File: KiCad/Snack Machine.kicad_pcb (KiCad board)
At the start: 2 copper layers, 107.5 x 100 mm, 318 parts, among them J1 MDB, J10 Row Screw Terminal, J11 Column Screw Terminal, J12 Display Serial Header, J13 RFID_CONNECTOR, J14 Large Display Header, J16 USB_B_Micro, J17 AVR-ISP-6, J18 Conn_02x02_Odd_Even, J2 Power Screw Terminal, J3 RFID Serial Connector, J4 RFID Led Connector, J5 MDB, J6 Conn_01x02, J7 LCD EXP1, J8 LCD EXP2, J9 AVR-ISP-6, Q1 P-CH 30V 3.8A, Q10 MMBT3904, Q11 P-CH 30V 3.8A, Q12 P-CH 30V 3.8A, Q13 P-CH 30V 3.8A, Q14 P-CH 30V 3.8A, Q15 MMBT3904, Q16 MMBT3904, Q17 MMBT3904, Q18 MMBT3904, Q19 Q_NMOS_SGD, Q2 Q_NMOS_SGD, Q20 Q_NMOS_SGD, Q21 Q_NMOS_SGD, Q22 Q_NMOS_SGD, Q23 Q_NMOS_SGD, Q24 Q_NMOS_SGD, Q25 Q_NMOS_SGD, Q26 MMBT3904, Q3 P-CH 30V 3.8A, Q4 P-CH 30V 3.8A, Q5 P-CH 30V 3.8A, Q6 P-CH 30V 3.8A, Q7 MMBT3904, Q8 MMBT3904, Q9 MMBT3904, SW1 SW_SPST, U1 MEZD71201A-F, U2 MEZD71202A-G, U3 ATmega2560-16AU, U4 INA180B3, U5 INA219, U6 ATmega16U2-MU, U7 74AHC1G125, U8 W5500, U9 RB1-125BAG1A, Y1 16MHz, Y2 16MHz, Y3 25MHz

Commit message: tweaked
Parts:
- moved C24 0.50 mm to (109.3, 84.9)
- moved C26 0.50 mm to (109.3, 86.6)
- moved F2 0.50 mm to (107.3, 90.3)
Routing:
- added copper zone on B.Cu, net GND
- removed copper zone on B.Cu, net (none)
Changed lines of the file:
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@@
     (thickness 1.6)
     (drawings 12)
-    (tracks 2542)
+    (tracks 2543)
     (zones 0)
     (modules 318)
@@
     (add_net /USB_Serial/TXL)
     (add_net /USB_Serial/TX_USB)
-    (add_net /USB_Serial/USBVCC)
     (add_net /USB_Serial/USB_D+)
     (add_net /USB_Serial/USB_D-)
@@
     (add_net +3V3)
     (add_net +5V)
+    (add_net /USB_Serial/USBVCC)
     (add_net GND)
     (add_net VCC)
@@
   )
   (module "Snack Machine:MF-MSMF050-2" (layer F.Cu)
-    (at 107.3 90.763 270)
+    (at 107.3 90.263 270)
     (fp_text reference F2 (at -0.1 3.9) (layer F.SilkS)
       (effects (font (size 1 1) (thickness 0.15)))
@@
   )
   (module Capacitor_SMD:C_0603_1608Metric_Pad1.05x0.95mm_HandSolder (layer F.Cu)
-    (at 109.3 85.363)
+    (at 109.3 84.863)
     (descr "Capacitor SMD 0603 (1608 Metric), square (rectangular) end terminal, IPC_7351 nominal with elongated pad for handsoldering. (Body size source: http://www.tortai-tech.com/upload/download/2011102023233369053.pdf), generated with kicad-footprint-generator")
     (tags "capacitor handsolder")
@@
   )
   (module Capacitor_SMD:C_0603_1608Metric_Pad1.05x0.95mm_HandSolder (layer F.Cu)
-    (at 109.3 87.063)
+    (at 109.3 86.563)
     (descr "Capacitor SMD 0603 (1608 Metric), square (rectangular) end terminal, IPC_7351 nominal with elongated pad for handsoldering. (Body size source: http://www.tortai-tech.com/upload/download/2011102023233369053.pdf), generated with kicad-footprint-generator")
     (tags "capacitor handsolder")
@@
   (segment (start 177.668 87.517) (end 178.054 87.131) (width 0.8) (layer F.Cu) (net 2))
   (segment (start 176.022 87.517) (end 177.668 87.517) (width 0.8) (layer F.Cu) (net 2))
-  (segment (start 116.6413 87.063) (end 118.2751 88.6968) (width 0.8) (layer F.Cu) (net 2))
-  (segment (start 110.175 87.063) (end 116.6413 87.063) (width 0.8) (layer F.Cu) (net 2))
-  (segment (start 110.175 85.363) (end 110.175 87.063) (width 0.8) (layer F.Cu) (net 2))
+  (segment (start 110.175 84.863) (end 110.175 86.563) (width 0.8) (layer F.Cu) (net 2))
   (segment (start 99.95 57.05) (end 96 57.05) (width 0.8) (layer F.Cu) (net 2))
   (segment (start 100.7999 57.8999) (end 99.95 57.05) (width 0.8) (layer F.Cu) (net 2))
@@
   (segment (start 196 142.95) (end 196 147.3) (width 0.8) (layer B.Cu) (net 2))
   (segment (start 196 147.3) (end 194.216 149.084) (width 0.8) (layer B.Cu) (net 2))
+  (segment (start 116.1413 86.563) (end 110.175 86.563) (width 0.8) (layer F.Cu) (net 2))
+  (segment (start 118.2751 88.6968) (end 116.1413 86.563) (width 0.8) (layer F.Cu) (net 2))
   (segment (start 154.2722 111.107) (end 149.6665 111.107) (width 0.25) (layer F.Cu) (net 3))
   (segment (start 156.379 110.277) (end 155.1022 110.277) (width 0.25) (layer F.Cu) (net 3))
@@
   (segment (start 112.16299 89.85591) (end 112.1856 89.8333) (width 0.25) (layer B.Cu) (net 13))
   (segment (start 105.823001 93.973901) (end 105.823001 86.488001) (width 0.8) (layer B.Cu) (net 14))
-  (segment (start 108.425 85.363) (end 108.425 87.063) (width 0.8) (layer F.Cu) (net 14))
-  (segment (start 106.398 87.063) (end 105.823001 86.488001) (width 0.8) (layer F.Cu) (net 14))
-  (segment (start 108.425 87.063) (end 106.398 87.063) (width 0.8) (layer F.Cu) (net 14))
+  (segment (start 108.425 84.863) (end 108.425 86.563) (width 0.8) (layer F.Cu) (net 14))
   (segment (start 106.7222 111.853) (end 106.7181 111.8489) (width 0.8) (layer F.Cu) (net 14))
   (segment (start 108.585 111.853) (end 106.7222 111.853) (width 0.8) (layer F.Cu) (net 14))
@@
   (segment (start 105.823001 93.973901) (end 104.387399 93.973901) (width 0.8) (layer B.Cu) (net 14))
   (segment (start 104.387399 93.973901) (end 102.9843 95.377) (width 0.8) (layer B.Cu) (net 14))
-  (segment (start 108.425 89.163) (end 107.3 89.163) (width 0.8) (layer F.Cu) (net 14))
-  (segment (start 108.425 87.063) (end 108.425 89.163) (width 0.8) (layer F.Cu) (net 14))
   (segment (start 107.1753 95.3262) (end 105.823001 93.973901) (width 0.25) (layer B.Cu) (net 14))
   (segment (start 110.5262 95.3262) (end 107.1753 95.3262) (width 0.25) (layer B.Cu) (net 14))
   (segment (start 113.052402 96.33091) (end 111.53091 96.33091) (width 0.25) (layer B.Cu) (net 14))
   (segment (start 111.53091 96.33091) (end 110.5262 95.3262) (width 0.25) (layer B.Cu) (net 14))
+  (segment (start 106.925001 86.488001) (end 105.823001 86.488001) (width 0.8) (layer F.Cu) (net 14))
+  (segment (start 108.425 86.563) (end 107 86.563) (width 0.8) (layer F.Cu) (net 14))
+  (segment (start 107 86.563) (end 106.925001 86.488001) (width 0.8) (layer F.Cu) (net 14))
+  (segment (start 108.425 88.663) (end 107.3 88.663) (width 0.8) (layer F.Cu) (net 14))
+  (segment (start 108.425 86.563) (end 108.425 88.663) (width 0.8) (layer F.Cu) (net 14))
   (segment (start 114.239902 92.159198) (end 114.286 92.1131) (width 0.25) (layer B.Cu) (net 15))
   (segment (start 114.239902 95.14341) (end 114.239902 92.159198) (width 0.25) (layer B.Cu) (net 15))
@@
   (segment (start 167.967537 123.17653) (end 167.967537 122.932463) (width 0.25) (layer B.Cu) (net 283))
   (segment (start 167.967537 122.932463) (end 168.7 122.2) (width 0.25) (layer B.Cu) (net 283))
-  (zone (net 0) (net_name "") (layer B.Cu) (hatch edge 0.508)
+  (zone (net 2) (net_name GND) (layer B.Cu) (hatch edge 0.508)
     (connect_pads (clearance 0.508))
     (min_thickness 0.254)
@@
     (polygon
       (pts
-        (xy 200.66 49.53) (xy 302.26 49.53) (xy 302.26 158.75) (xy 200.66 158.75)
+        (xy 99.360496 49) (xy 200.960496 49) (xy 200.960496 158.22) (xy 99.360496 158.22)
       )
     )

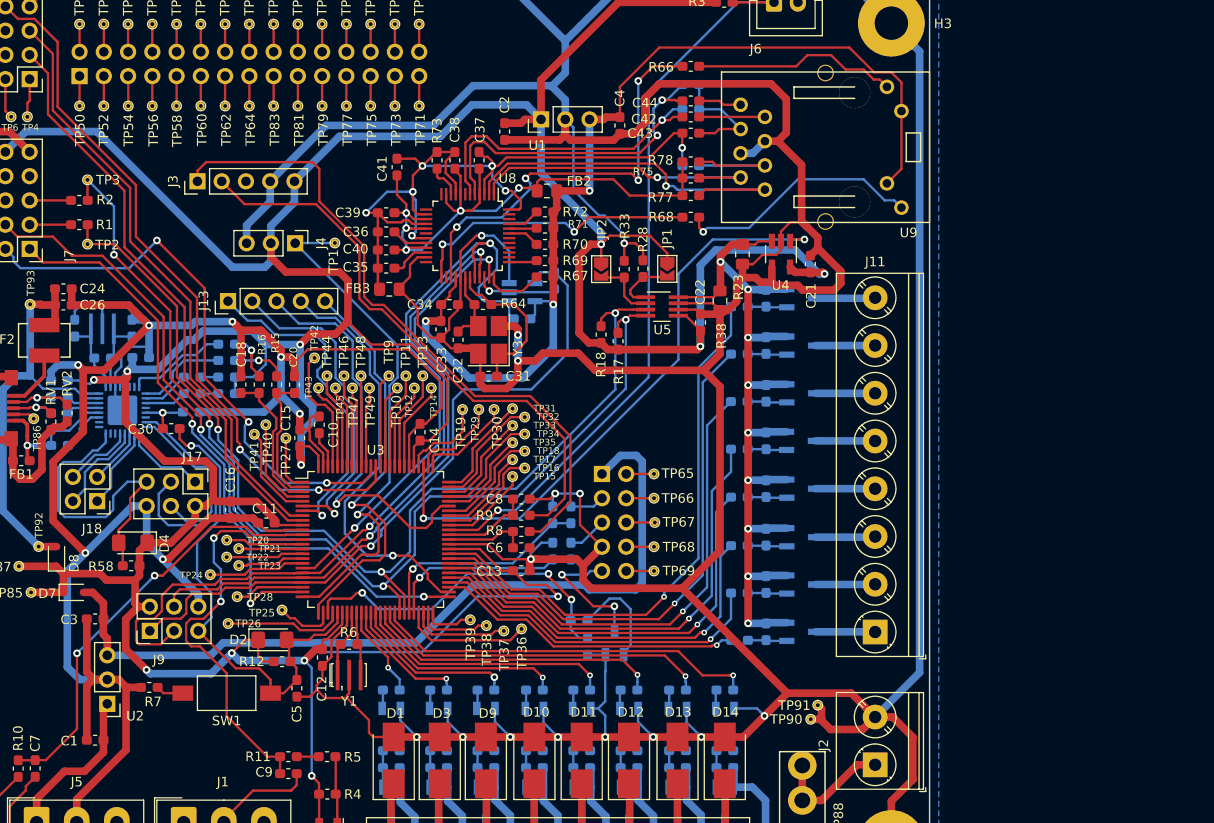
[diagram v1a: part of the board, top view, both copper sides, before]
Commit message: imported new netlist
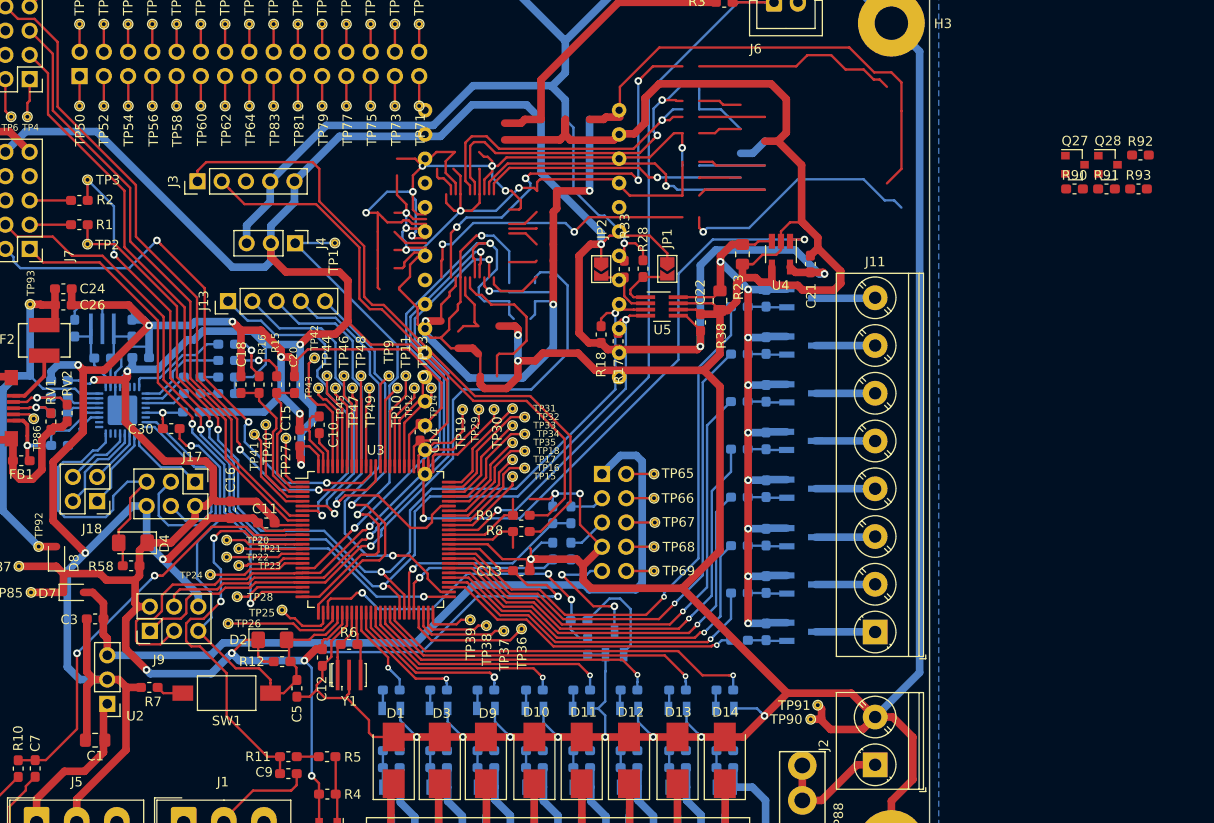
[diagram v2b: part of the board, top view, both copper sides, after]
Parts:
- removed C2: 2.2uF 10V, Capacitor_SMD:C_0603_1608Metric_Pad1.05x0.95mm_HandSolder
- removed C31, C32: 22pF, Capacitor_SMD:C_0603_1608Metric_Pad1.05x0.95mm_HandSolder
- removed C33, C36, C41: 10uF, Capacitor_SMD:C_0603_1608Metric_Pad1.05x0.95mm_HandSolder
- removed C34, C35, C37, C38, C39, C40: 0.1uF, Capacitor_SMD:C_0603_1608Metric_Pad1.05x0.95mm_HandSolder
- removed C4: 10uF 10V, Capacitor_SMD:C_0603_1608Metric_Pad1.05x0.95mm_HandSolder
- removed C42, C44: 6.8nF, Capacitor_SMD:C_0603_1608Metric_Pad1.05x0.95mm_HandSolder
- removed C43, C45: 10nF, Capacitor_SMD:C_0603_1608Metric_Pad1.05x0.95mm_HandSolder
- removed C6, C8: OPEN, Capacitor_SMD:C_0603_1608Metric_Pad1.05x0.95mm_HandSolder
- removed FB2, FB3: Ferrite_Bead, Inductor_SMD:L_0805_2012Metric_Pad1.15x1.40mm_HandSolder
- removed R64: 1M, Resistor_SMD:R_0603_1608Metric_Pad1.05x0.95mm_HandSolder
- removed R65: 10K, Resistor_SMD:R_0603_1608Metric_Pad1.05x0.95mm_HandSolder
- removed R66, R68: 470, Resistor_SMD:R_0603_1608Metric_Pad1.05x0.95mm_HandSolder
- removed R67, R69, R70, R71, R72: 10k, Resistor_SMD:R_0603_1608Metric_Pad1.05x0.95mm_HandSolder
- removed R73: 12.1k, Resistor_SMD:R_0603_1608Metric_Pad1.05x0.95mm_HandSolder
- removed R74, R75, R76, R77: 49.9, Resistor_SMD:R_0603_1608Metric_Pad1.05x0.95mm_HandSolder
- removed R78: 10, Resistor_SMD:R_0603_1608Metric_Pad1.05x0.95mm_HandSolder
- removed R87: OPEN, Resistor_SMD:R_0603_1608Metric_Pad1.05x0.95mm_HandSolder
- removed U1: MEZD71201A-F, Snack Machine:mEZD71201A
- removed U8: W5500, Package_QFP:TQFP-48_7x7mm_P0.5mm
- removed U9: RB1-125BAG1A, Snack Machine:RB1-125BAG1A
- removed Y3: 25MHz, Crystal:Crystal_SMD_SeikoEpson_TSX3225-4Pin_3.2x2.5mm_HandSoldering
- added Q27: BSS138, Package_TO_SOT_SMD:SOT-23, F.Cu at (215.2, 71.9)
- added Q28: BSS138, Package_TO_SOT_SMD:SOT-23, F.Cu at (218.7, 71.9)
- added R90: 10k, Resistor_SMD:R_0603_1608Metric_Pad1.05x0.95mm_HandSolder, F.Cu at (215.2, 74.4)
- added R91: 10k, Resistor_SMD:R_0603_1608Metric_Pad1.05x0.95mm_HandSolder, F.Cu at (218.5, 74.4)
- added R92: 10k, Resistor_SMD:R_0603_1608Metric_Pad1.05x0.95mm_HandSolder, F.Cu at (222.1, 70.9)
- added R93: 10k, Resistor_SMD:R_0603_1608Metric_Pad1.05x0.95mm_HandSolder, F.Cu at (221.9, 74.4)
- C1: footprint Capacitor_SMD:C_0603_1608Metric_Pad1.05x0.95mm_HandSolder -> Capacitor_SMD:C_0805_2012Metric_Pad1.15x1.40mm_HandSolder
- R12, R3, R4: value 10K -> 10k
- R17, R18, R5: value 1K -> 1k
- R58: value R -> 10k
- U7: value 74AHC1G125 -> Huzzah32; footprint Package_TO_SOT_SMD:SOT-23-5_HandSoldering -> Snack Machine:HUZZAH32
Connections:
- J12 pad 3: /RX_DISPLAY -> /TX_DISPLAY
- J12 pad 5: /TX_DISPLAY -> /RX_DISPLAY
- R13 pad 1: /RX_DISPLAY -> /TX_DISPLAY
- R14 pad 1: /TX_DISPLAY -> /RX_DISPLAY
- R8 pad 1: /RFID_TX -> /RFID_RX
- R8 pad 2: Net-(C6-Pad1) -> Net-(C17-Pad1)
- R9 pad 1: /RFID_RX -> /RFID_TX
- R9 pad 2: Net-(C8-Pad1) -> Net-(C19-Pad1)
- U3 pad 63: Net-(C6-Pad1) -> Net-(Q27-Pad3)
- U3 pad 64: Net-(C8-Pad1) -> Net-(Q28-Pad3)
- U7 pad 1: /CS -> Net-(U7-Pad1)
- U7 pad 2: /Ethernet/MISO_TRISTATE -> Net-(U7-Pad2)
- U7 pad 3: GND -> +5V
- U7 pad 4: /MISO -> Net-(U7-Pad4)
- U7 pad 5: +3V3 -> Net-(U7-Pad5)
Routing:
- net +3V3: track 106.7 -> 0.00 mm, vias 3 -> 0
- net Net-(U7-Pad22): track 0.00 -> 56.3 mm, vias 0 -> 3
- net Net-(U7-Pad12): track 0.00 -> 50.3 mm
- net /TX_DISPLAY: track 4.13 -> 3.61 mm
- net /RX_DISPLAY: track 3.61 -> 4.13 mm

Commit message: I think all traces are routed, about to run DRC
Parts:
- Q27, Q28, R90, R91, R92, R93: moved to B.Cu
- U7: moved to F.Cu
- moved R91 64.8 mm to (155.5, 89.8)
- moved R93 60.9 mm to (162.9, 89.8)
- moved Q27 60.7 mm to (156.4, 87.1), turned to 270 degrees
- moved R92 59.8 mm to (163.8, 84.4)
- moved R90 59.6 mm to (156.4, 84.4)
- moved Q28 56.9 mm to (163.8, 87.1), turned to 270 degrees
- moved R18 26.2 mm to (175.8, 65.5), turned to 0 degrees
- moved R17 24.3 mm to (175.1, 67.3), turned to 0 degrees
- moved JP2 24.3 mm to (182.7, 65.5), turned to 180 degrees
- moved R33 20.9 mm to (182.7, 67.9), turned to 0 degrees
- moved R28 18.1 mm to (182.7, 69.9), turned to 0 degrees
- moved U5 16.3 mm to (178.8, 71.9), turned to 270 degrees
- moved JP1 14.5 mm to (182.7, 72.4), turned to 180 degrees
- moved C22 12.5 mm to (177.1, 75.9), turned to 0 degrees
- moved U7 10.1 mm to (160.9, 75.8), turned to 180 degrees
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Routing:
- net GND: track 1099.9 -> 966.3 mm, vias 22 -> 17
- net /Ethernet/AGND: track 91.1 -> 0.00 mm, vias 7 -> 0
- net /Ethernet/AVDD: track 68.1 -> 0.00 mm, vias 5 -> 0
- net /CS: track 63.7 -> 0.00 mm, vias 2 -> 0
- net Net-(U7-Pad22): track 56.3 -> 0.00 mm, vias 3 -> 0
- net /MISO: track 72.4 -> 18.9 mm, vias 1 -> 0
- net Net-(U7-Pad12): track 50.3 -> 0.00 mm
- net /MOSI: track 64.1 -> 15.4 mm, vias 2 -> 0
- net /SCK: track 75.8 -> 27.3 mm, vias 2 -> 0
- net Net-(R66-Pad1): track 44.1 -> 0.00 mm, vias 4 -> 0
- net Net-(Q28-Pad3): track 0.00 -> 41.7 mm, vias 0 -> 1
- net /Ethernet/TX+: track 39.9 -> 0.00 mm, vias 1 -> 0
- net Net-(Q27-Pad3): track 0.00 -> 37.0 mm, vias 0 -> 1
- net /Ethernet/RX-: track 35.5 -> 0.00 mm, vias 2 -> 0
- net /Ethernet/RX+: track 33.1 -> 0.00 mm, vias 1 -> 0
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
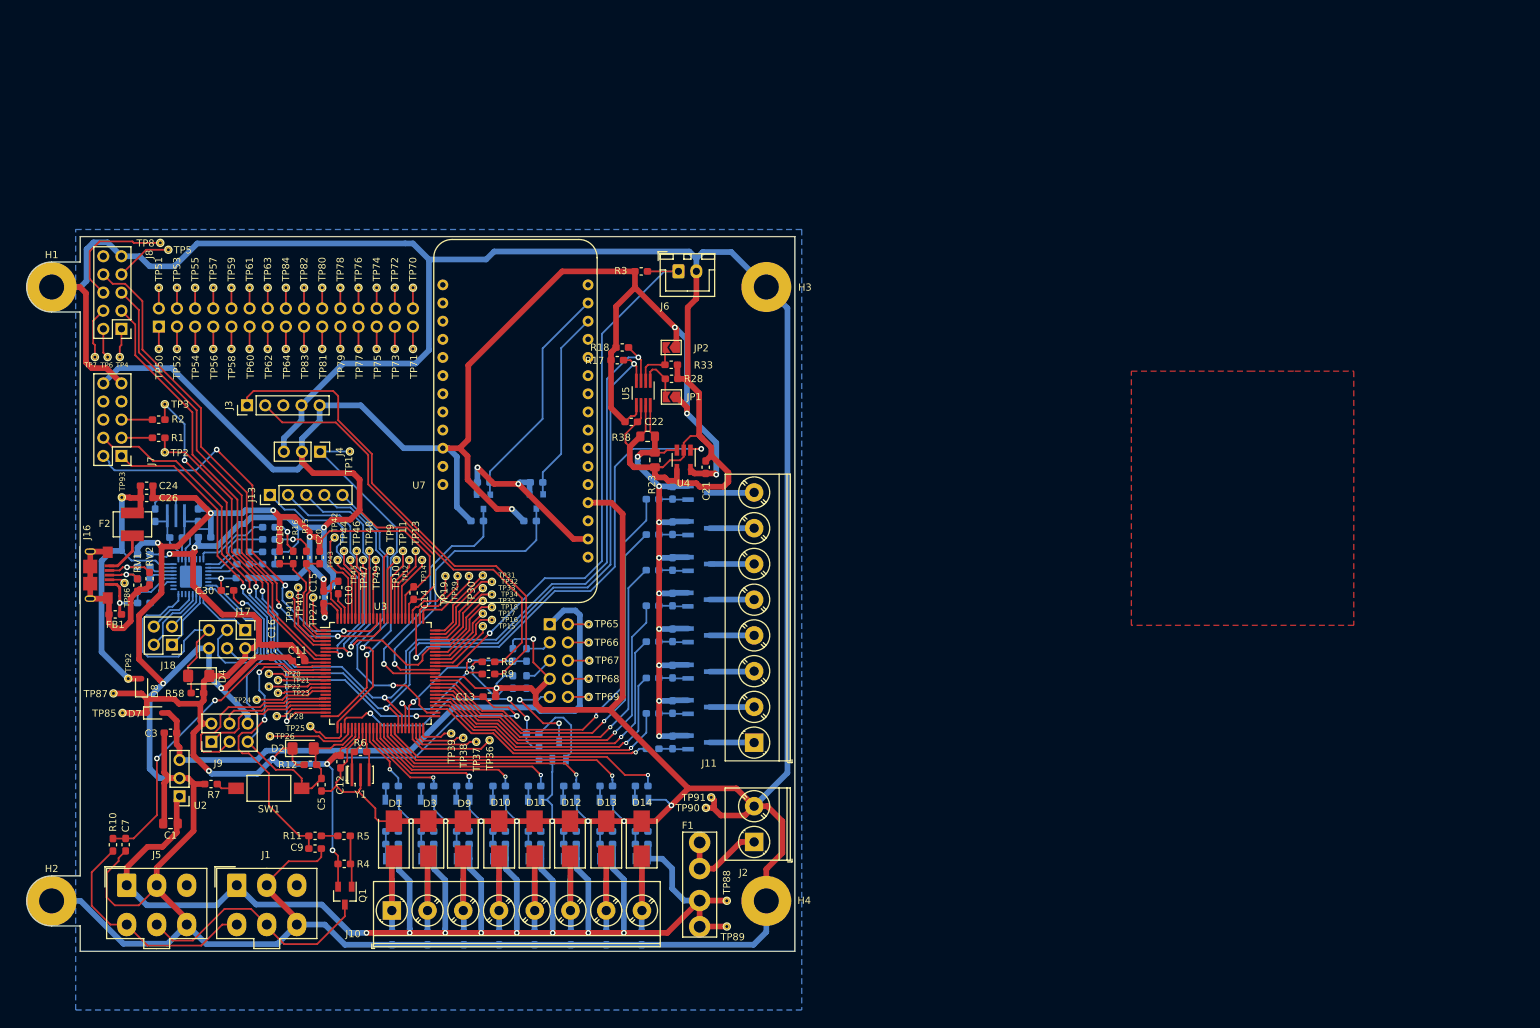
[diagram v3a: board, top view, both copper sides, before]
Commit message: pushed a couple of reference designators, fixed copper pours
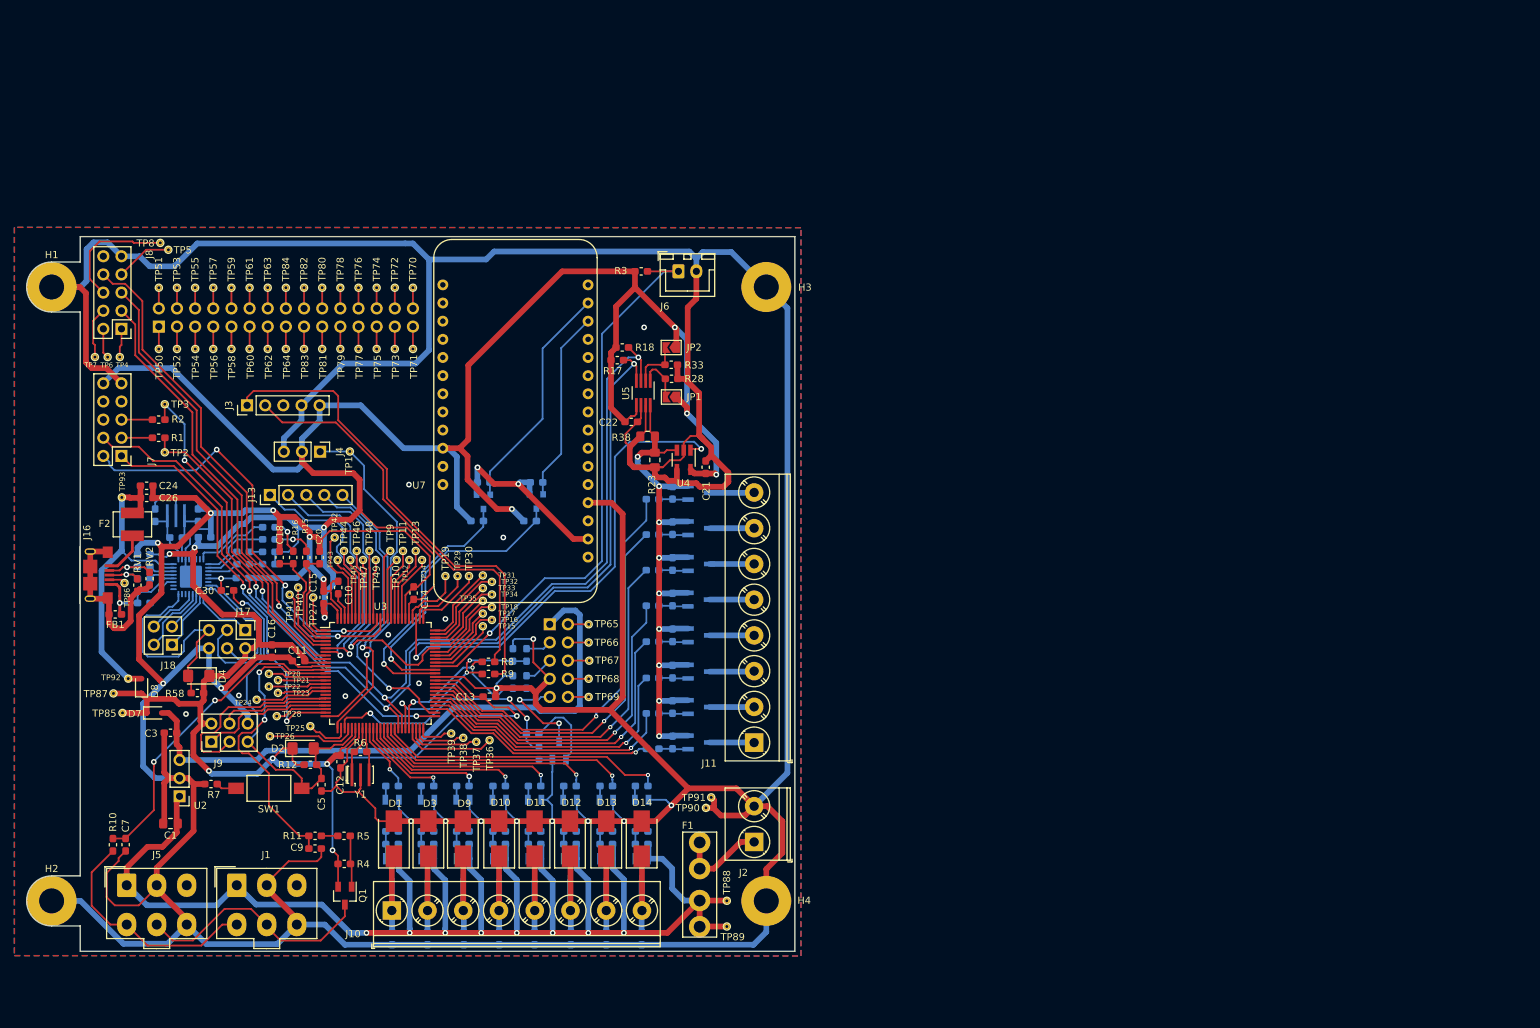
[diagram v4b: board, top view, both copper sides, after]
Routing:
- net /RFID_RX: track 60.6 -> 57.4 mm
- net /SCL: track 141.9 -> 138.9 mm
- net /LCD_CS: track 70.5 -> 67.5 mm
- net /SDA: track 139.1 -> 136.2 mm
- net /RFID_TX: track 70.1 -> 67.6 mm
- net /RFID_LED: track 50.8 -> 49.1 mm
- net /MOTOR_CURRENT: track 67.2 -> 68.9 mm
- net /RFID_RED_LED: track 44.3 -> 43.1 mm
- net GND: track 966.3 -> 967.4 mm, vias 17 -> 26
- net /USB_Serial/USBVCC: track 46.6 -> 45.8 mm
- net Net-(Q28-Pad3): track 41.7 -> 41.1 mm
- net Net-(C7-Pad1): track 44.9 -> 44.3 mm
- net Net-(Q27-Pad3): track 37.0 -> 36.5 mm
- added copper zone on F.Cu, net GND
- removed copper zone on F.Cu, net /Ethernet/AGND

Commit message: created gerbers
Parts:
- added G***: LOGO, Snack Machine:TGD-logo, F.Cu at (185.0, 106.3)
- added G***: LOGO, Snack Machine:denhac-logo, F.Cu at (185.5, 119.0)
- added G***: LOGO, Snack Machine:oshw-logo, F.Cu at (185.4, 92.3)
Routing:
- net /~RESET: track 52.1 -> 52.8 mm
- net +5V: track 473.9 -> 473.4 mm
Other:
- board text added: "Snack Machine Controller v1.0"
